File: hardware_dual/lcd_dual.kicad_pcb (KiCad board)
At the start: 2 copper layers, 80 x 50 mm, 128 parts, among them J1 HDMI-A receptacle, J2 USB-C (power + touch USB), J3 AT070TN92 FPC (0.5mm 50P, top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, J4 Touch FPC 6P 0.5mm, J5 SWD/UART, Q1 AO3401A, Q2 2N7002, SW1 BOOT (DFU), SW2 BOOT CH32, U1 LT8619C, U10 STM32F072CBT6 / CH32X035C8T6, U2 AMS1117-3.3, U3 AMS1117-1.8, U4 USBLC6-2SC6, U7 TPS61040, U8 LM321, U9 TPS61165, Y1 25MHz 12pF

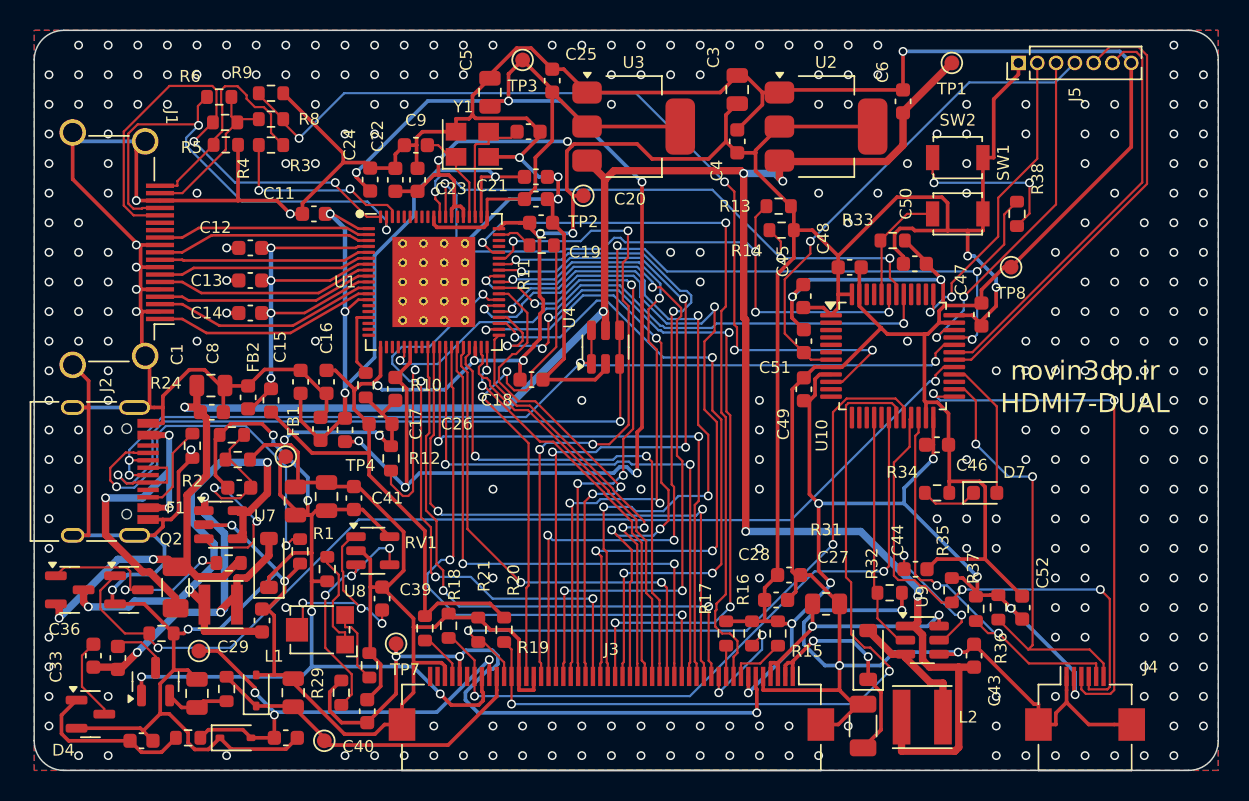
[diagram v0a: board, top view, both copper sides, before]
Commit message: Dual board: vias 0.7 mm pad / 0.4 mm drill
All 463 vias are now 0.7 mm outer diameter with a 0.4 mm hole (0.15 mm
annular ring). The board was fully rerouted for the larger pads.
DRC 0 errors, 0 unconnected, netlist matches design.py.

Co-Authored-By: Claude Opus 5.5 <noreply@anthropic.com>
Claude-Session: https://claude.ai/code/session_01X8BrieHZtCS6HfoR48ML9y
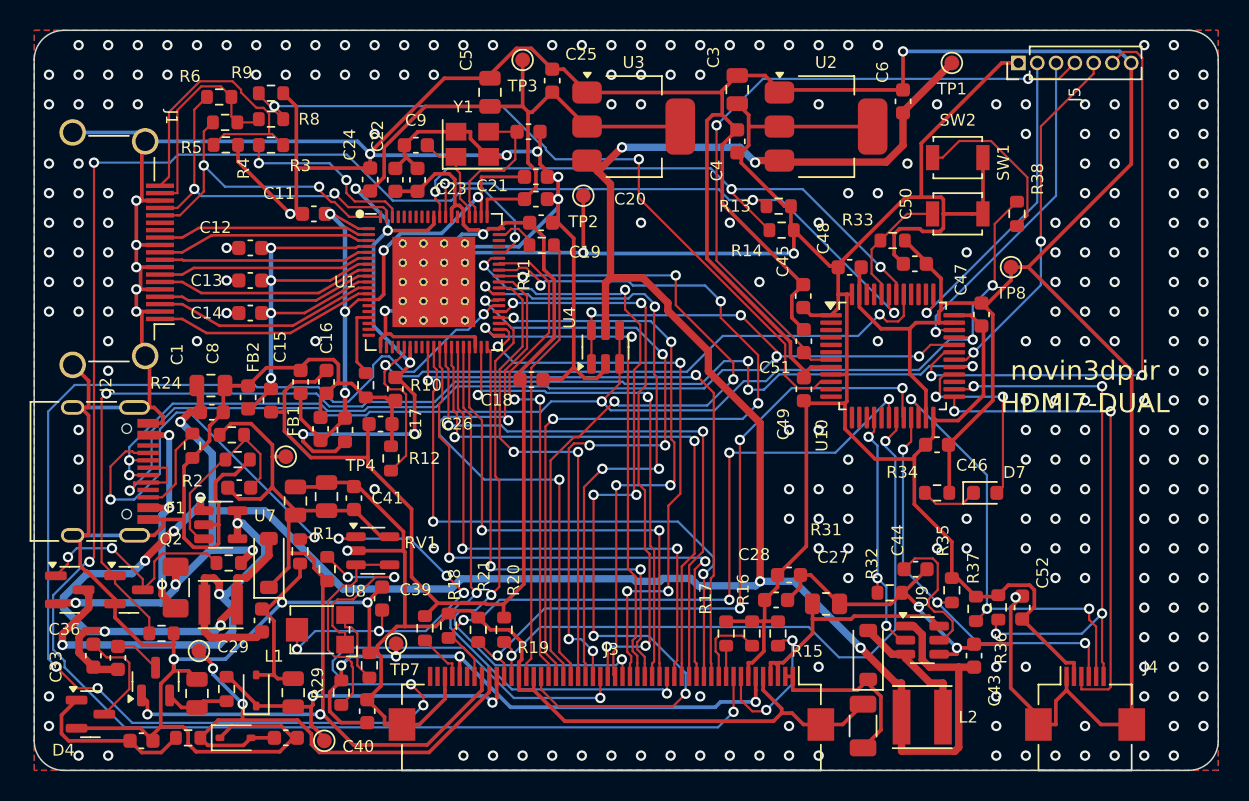
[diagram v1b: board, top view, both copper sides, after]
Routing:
- net LCD_DE: track 50.6 -> 119.4 mm, vias 2 -> 4
- net LCD_G0: track 54.6 -> 109.4 mm, vias 4 -> 6
- net GND: track 569.6 -> 618.2 mm, vias 310 -> 262
- net +1V8: track 110.8 -> 76.6 mm, vias 6 -> 5
- net LCD_R1: track 50.2 -> 33.8 mm, vias 4 -> 2
- net USB_DM: track 66.5 -> 81.0 mm, vias 4 -> 6
- net LCD_G2: track 53.2 -> 38.9 mm, vias 6 -> 4
- net LCD_R0: track 45.4 -> 58.8 mm, vias 4 -> 6
- net UART_RX: track 28.4 -> 40.8 mm, vias 0 -> 2
- net HDMI_SCL: track 34.3 -> 22.1 mm
- net AVDD_SW: track 27.1 -> 39.3 mm, vias 3 -> 5
- net MCU_NRST: track 33.7 -> 45.8 mm, vias 1 -> 2
- net BIAS_EN: track 69.8 -> 81.8 mm, vias 2 -> 4
- net VCOM_SET: track 14.9 -> 26.9 mm, vias 3 -> 5
- net LCD_G1: track 48.3 -> 38.5 mm
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
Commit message: Dual board: TPS61169DCKR backlight driver
- U9 TPS61165 (SOT-23-6) -> TPS61169DCKR (SC70-5) per the TI datasheet:
  1 SW, 2 GND, 3 FB, 4 CTRL, 5 VIN; new project symbol; internal
  compensation, so C44 is removed.
- R31 1.13 R 1%: 204 mV reference -> 180 mA LED current.
- 20 kHz PWM on CTRL (datasheet 5..100 kHz), 10 uH inductor (4.7..10 uH),
  2.2 uF output capacitor (1..10 uF) are unchanged; firmware unchanged.
- Rerouted (0.7/0.4 vias): first pass plus a second pass for the last
  net (lcd_dual_stage2.ses); route.py import now prunes unused stubs.
  DRC 0 errors, 0 unconnected, netlist matches design.py.

Co-Authored-By: Claude Opus 5.5 <noreply@anthropic.com>
Claude-Session: https://claude.ai/code/session_01X8BrieHZtCS6HfoR48ML9y
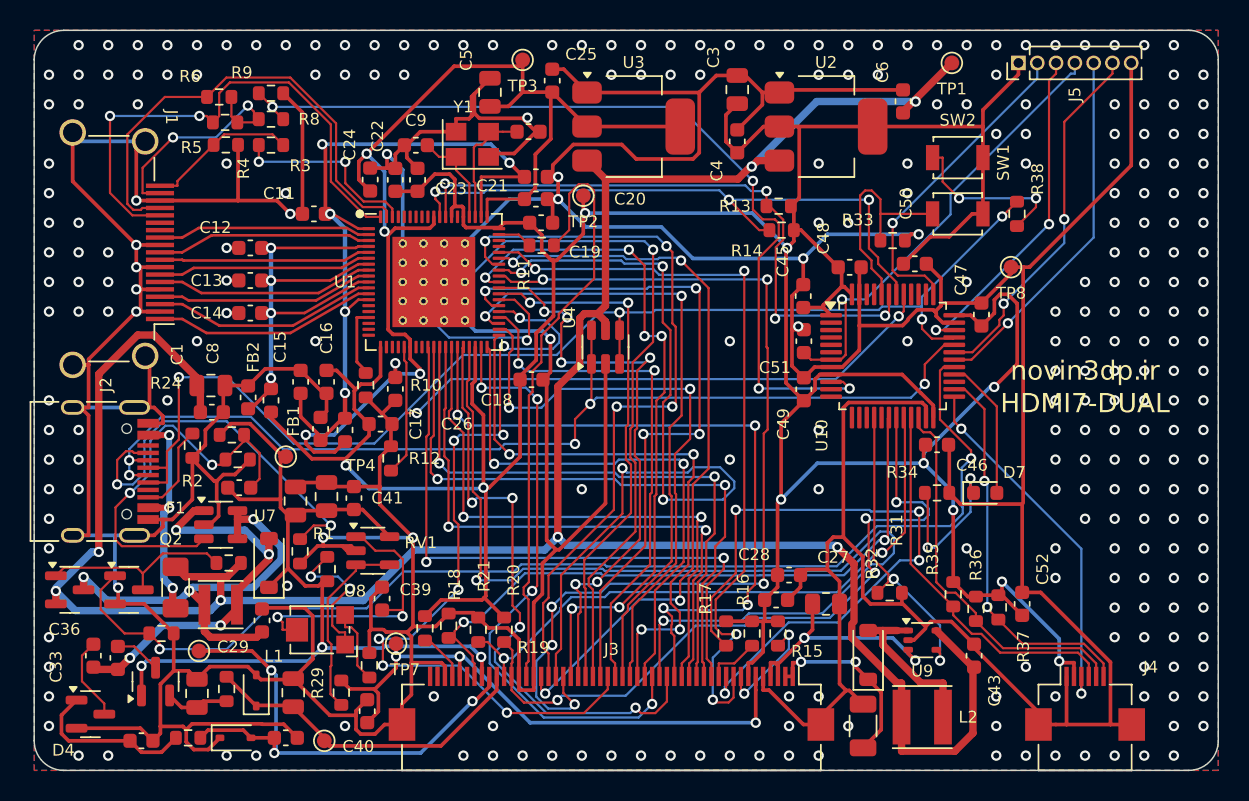
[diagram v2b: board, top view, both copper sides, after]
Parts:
- removed C44: 220nF, Capacitor_SMD:C_0603_1608Metric
- R31: value 1.1R 1% -> 1.13R 1%
- U9: value TPS61165 -> TPS61169DCKR; footprint Package_TO_SOT_SMD:SOT-23-6 -> Package_TO_SOT_SMD:SOT-353_SC-70-5
- moved R35 0.29 mm to (162.1, 118.1)
- moved C52 0.25 mm to (166.8, 118.8)
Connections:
- U9 pad 1: +5V -> BL_SW
- U9 pad 2: BL_PWM -> GND
- U9 pad 3: BL_SW -> VLED_K
- U9 pad 4: GND -> BL_PWM
- U9 pad 5: BL_COMP -> +5V
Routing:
- net LCD_DE: track 119.4 -> 51.9 mm
- net LCD_G0: track 109.4 -> 47.5 mm, vias 6 -> 4
- net LCD_VS: track 2.08 -> 44.4 mm, vias 0 -> 4
- net LCD_B0: track 34.6 -> 68.6 mm
- net LCD_G1: track 38.5 -> 55.8 mm, vias 4 -> 8
- net LCD_R1: track 33.8 -> 50.2 mm, vias 2 -> 4
- net LCD_R7: track 44.0 -> 60.3 mm, vias 6 -> 2
- net UART_RX: track 40.8 -> 24.7 mm
- net LCD_R3: track 50.4 -> 65.7 mm, vias 4 -> 6
- net MCU_NRST: track 45.8 -> 30.6 mm, vias 2 -> 1
- net AVDD_FB: track 13.2 -> 26.9 mm, vias 0 -> 2
- net HDMI_SCL: track 22.1 -> 35.7 mm
- net AVDD_SW: track 39.3 -> 26.2 mm, vias 5 -> 4
- net TP_RST: track 38.5 -> 26.4 mm, vias 4 -> 2
- net LCD_B2: track 37.0 -> 48.1 mm, vias 2 -> 4
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
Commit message: Dual board: Q1 AO3401A -> AO3415
Checked against the AOS AO3415 datasheet (Rev 7): -20 V VDS, +/-8 V VGS
(the gate only sees 0 / -5 V), RDS(on) < 41 mOhm at -4.5 V, same SOT-23
pinout (1 G, 2 S, 3 D). Footprint and routing unchanged; schematic
and BOM updated (the AO3401A LCSC number is dropped).

Co-Authored-By: Claude Opus 5.5 <noreply@anthropic.com>
Claude-Session: https://claude.ai/code/session_01X8BrieHZtCS6HfoR48ML9y
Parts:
- Q1: value AO3401A -> AO3415
